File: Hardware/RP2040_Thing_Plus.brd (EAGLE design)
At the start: 22.9 x 58.4 mm, 131 parts, among them J1 SWD, J3 Qwiic, J5 USB C, J6 microSD, Q1 20V/4.2A/52mΩ/1.4W, U2 MAX17048, U3 MCP73831, U4 W25QXX128MBIT, U5 RP2040, U6 WS2812-2020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

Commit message: Add TPs to SWD. Connect reset. v11.
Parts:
- added TP1, TP2, TP3: (no value), SparkFun-Connectors:PAD.03X.04
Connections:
- removed net !RESET: J1.10, J7.1, S2.3
- net !RESET!: now also J1.10, J7.1, S2.3, TP3.P$1
- net SWDCK: now also TP1.P$1
- net SWDIO: now also TP2.P$1
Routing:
- net !RESET!: track 0.00 -> 47.1 mm, vias 0 -> 2
- net !RESET: track 33.3 -> 0.00 mm, vias 1 -> 0
- net SWDCK: track 8.69 -> 23.3 mm
- net SWDIO: track 6.07 -> 18.4 mm
- net V_BATT: track 35.3 -> 34.8 mm
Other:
- board text added: "v11"
- board text removed: "v10"

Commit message: Add RP2040 Logo
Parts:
- removed U$43: (no value), output:RP20401
- removed U$46: (no value), output:RP2040_1
- added U$29: (no value), RP2040:RP2040_10
- added U$30: (no value), RP2040:RP2040_20

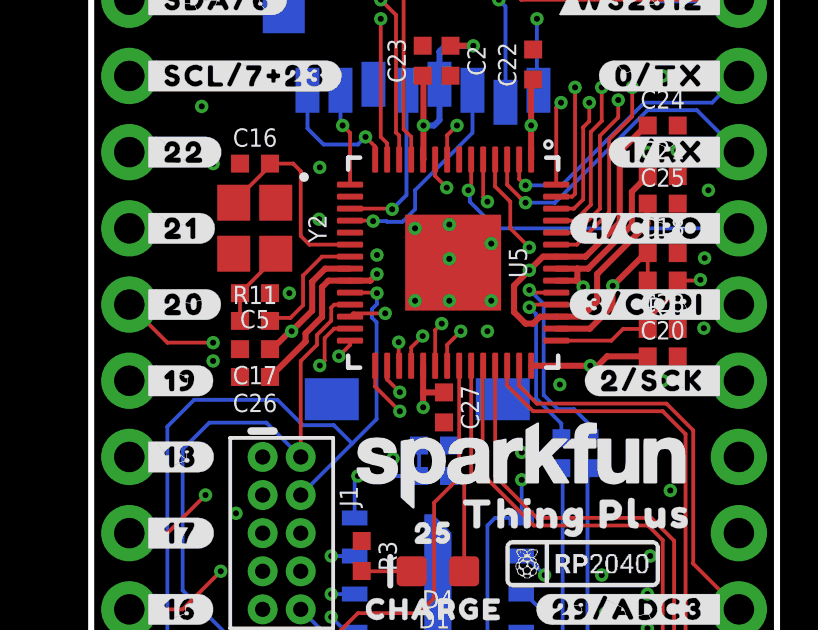
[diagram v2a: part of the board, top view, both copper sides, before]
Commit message: Update RP2040 Logo
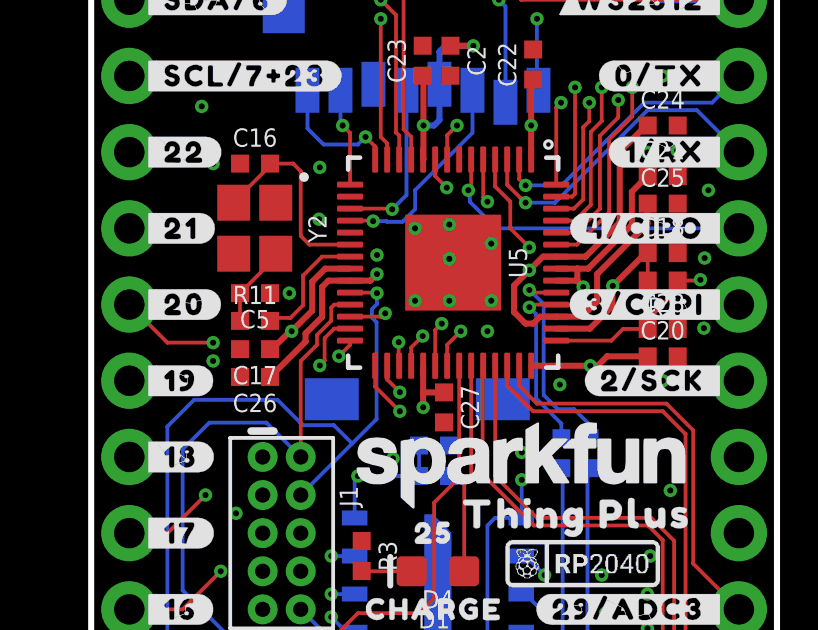
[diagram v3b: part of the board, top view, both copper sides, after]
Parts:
- moved U$30 1.15 mm to (5.84, 14.5)
- moved U$44 0.77 mm to (6.35, 17.1)
- moved U$32 0.52 mm to (9.02, 18.9)

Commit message: Added ARM DevSummit Logo
Removed logos from bottom of PCB and replaced with ARM DevSummit logo.
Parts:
- removed U$32: (no value), SparkFun-Aesthetics:SFE_LOGO_NAME_FLAME_.1
- removed U$44: (no value), output:THING_PLUS0
- U$30: device RP2040:RP2040_20 -> ARM1848_DevSummit_2021_Logos_ST3_Stacked#black#jpg (3):ARM1848_DEVSUMMIT_2021_LOGOS_ST3_STACKED#BLACK#JPG
- moved U$30 6.65 mm to (10.7, 19.1), turned to 90 degrees
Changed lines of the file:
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@@
 <element name="U$60" library="output" package="#WS2812#0" value="" x="11.43" y="56.642" smashed="yes"/>
 <element name="U$64" library="SparkFun-Aesthetics" package="QWIIC_4MM" value="" x="6.731" y="9.398" smashed="yes" rot="R270"/>
-<element name="U$32" library="SparkFun-Aesthetics" package="SFE_LOGO_NAME_FLAME_.1" value="" x="9.017" y="18.923" smashed="yes" rot="MR0"/>
 <element name="U$54" library="output" package="250" value="" x="11.43" y="34.29" smashed="yes"/>
 <element name="U$55" library="output" package="CHARGE0" value="" x="11.43" y="31.75" smashed="yes"/>
@@
 <element name="U$45" library="SparkFun-Aesthetics" package="SFE_LOGO_NAME_.1" value="" x="14.351" y="36.5506" smashed="yes"/>
 <element name="U$47" library="output" package="THING_PLUS_0" value="" x="16.383" y="34.925" smashed="yes"/>
-<element name="U$44" library="output" package="THING_PLUS0" value="" x="6.35" y="17.145" smashed="yes" rot="MR0"/>
 <element name="TP1" library="SparkFun-Connectors" package="PAD.03X.04" value="" x="2.54" y="30.48" smashed="yes" rot="MR0"/>
 <element name="TP2" library="SparkFun-Connectors" package="PAD.03X.04" value="" x="5.08" y="30.48" smashed="yes" rot="MR0"/>
 <element name="TP3" library="SparkFun-Connectors" package="PAD.03X.04" value="" x="7.62" y="30.48" smashed="yes" rot="MR0"/>
-<element name="U$30" library="RP2040" package="RP2040_20" value="" x="5.842" y="14.478" smashed="yes" rot="MR0"/>
 <element name="U$29" library="RP2040" package="RP2040_10" value="" x="16.383" y="33.274" smashed="yes"/>
+<element name="U$30" library="ARM1848_DevSummit_2021_Logos_ST3_Stacked#black#jpg (3)" package="ARM1848_DEVSUMMIT_2021_LOGOS_ST3_STACKED#BLACK#JPG" value="" x="10.668" y="19.05" smashed="yes" rot="MR90"/>
 </elements>
 <signals>
